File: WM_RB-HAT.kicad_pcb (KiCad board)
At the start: 4 copper layers, 65 x 40.5 mm, 61 parts, among them J1 AudioJack3, J2 AudioJack3, J3 2x20 Pins, J4 AudioJack3, J5 AudioJack3, J6 Audio In, J7 Audio Out, Q1 BC817, U1 WM8960, U4 MCP1711T-33 /OT

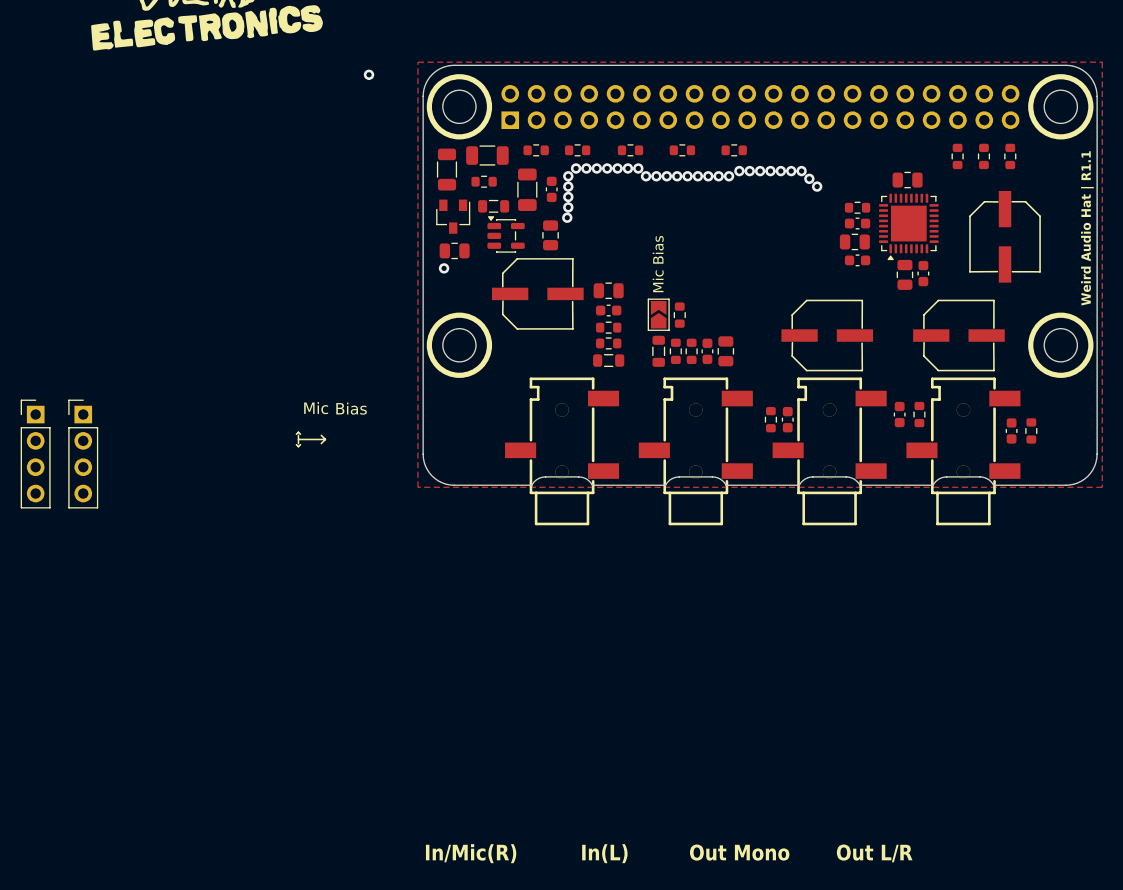
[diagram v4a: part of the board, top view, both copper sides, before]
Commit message: Resize PCB to Raspberry Pi Zero footprint
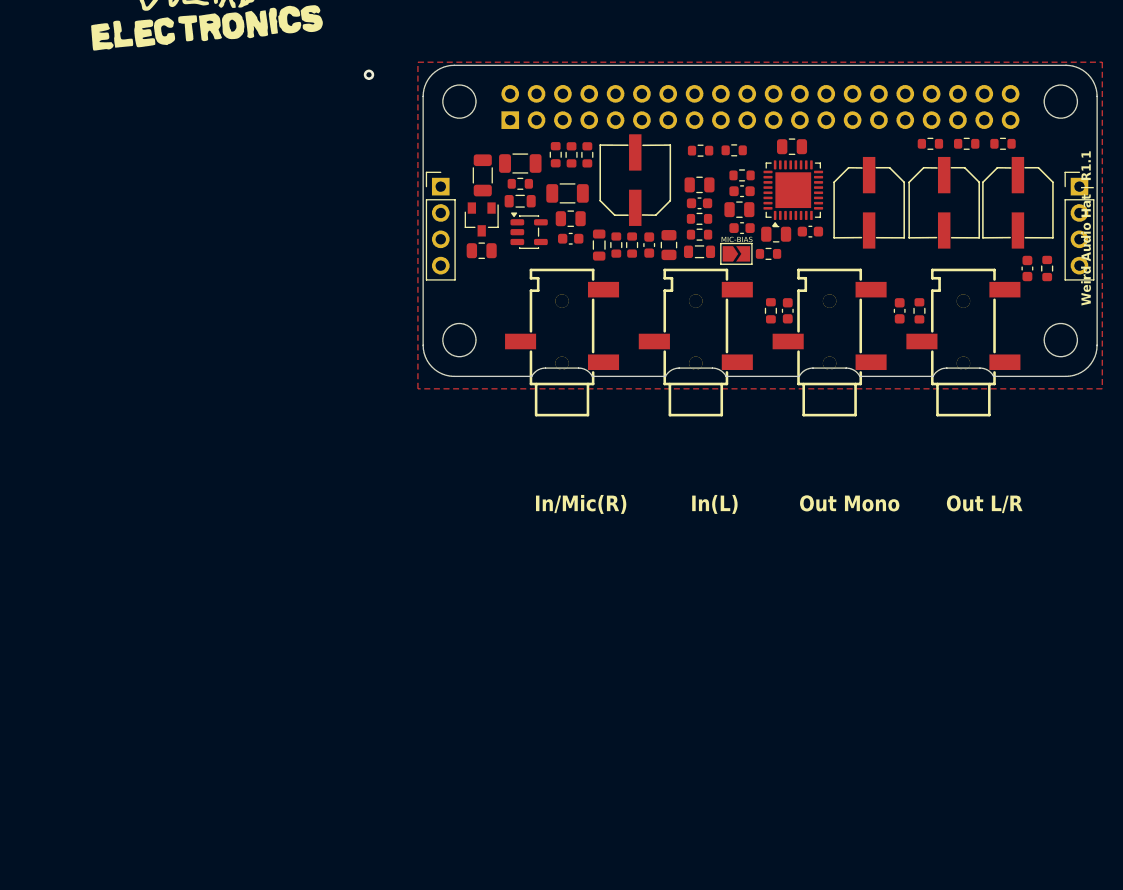
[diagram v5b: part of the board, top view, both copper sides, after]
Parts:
- JP1: value Mic Bias -> MIC-BIAS
- moved J7 98.6 mm to (141.8, 72.0)
- moved J6 44.8 mm to (80.2, 72.0)
- moved C18 16.3 mm to (105.2, 71.8), turned to 180 degrees
- moved C29 15.7 mm to (136.8, 79.9)
- moved R22 15.7 mm to (138.7, 79.9)
- moved CP3 14.4 mm to (99.0, 71.4), turned to 90 degrees
- moved C21 14.3 mm to (105.2, 73.6), turned to 0 degrees
- moved CP2 14.0 mm to (135.9, 73.6), turned to -90 degrees
- moved CP4 13.4 mm to (121.5, 73.6), turned to -90 degrees
- moved C2 13.0 mm to (112.5, 76.6), turned to 0 degrees
- moved R8 12.8 mm to (105.2, 75.1), turned to 0 degrees
- moved C3 11.6 mm to (115.8, 76.3), turned to 180 degrees
- moved C8 11.6 mm to (114.1, 68.1)
- moved U1 11.6 mm to (114.2, 72.3)
- moved C5 11.6 mm to (109.3, 76.0)
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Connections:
- J6 pad 2: /INPUT_R -> /LINE_INPUT_R
- J6 pad 4: /INPUT_L -> /LINE_INPUT_L
- J7 pad 2: /OUTPUT_R -> /HP_R_AC
- J7 pad 4: /OUTPUT_L -> /HP_L_AC
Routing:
- net GND: vias 32 -> 1
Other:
- board size 65 x 40.5 mm -> 65 x 30 mm
- board text removed: "Bias"
- board text removed: "Mic"

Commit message: PCB layout adjustments
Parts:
- G*** (x2): moved to B.Cu
- moved G*** 61.2 mm to (112.1, 81.0), turned to 172 degrees
- moved G*** 52.8 mm to (109.9, 73.6), turned to 180 degrees

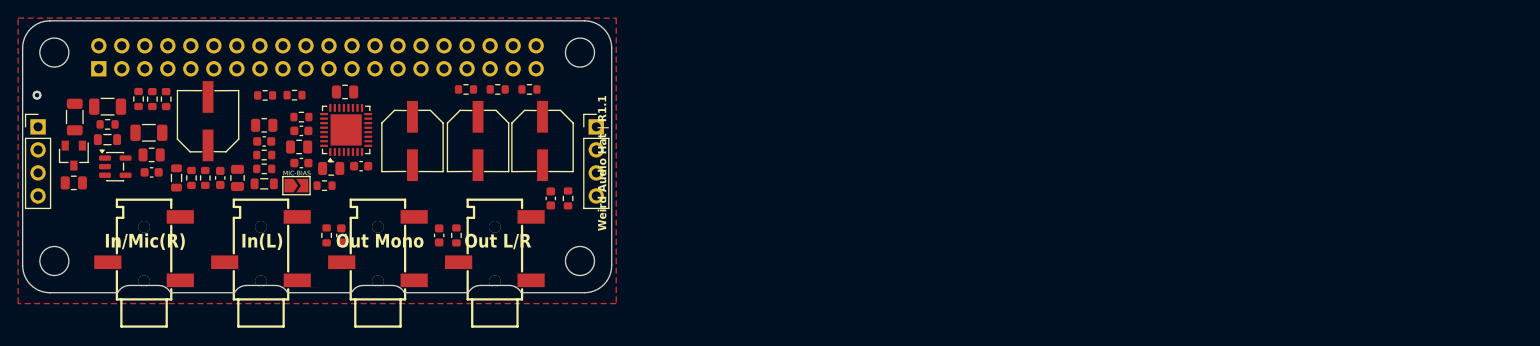
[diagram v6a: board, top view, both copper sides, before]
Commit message: Add SSSS213202 slide switch library, PCB and schematic updates
- Add Alps SSSS213202 SPDT switch: symbol, footprint, 3D model (LCSC C115375)
- Register switch libraries in sym-lib-table and fp-lib-table
- Schematic and PCB layout updates
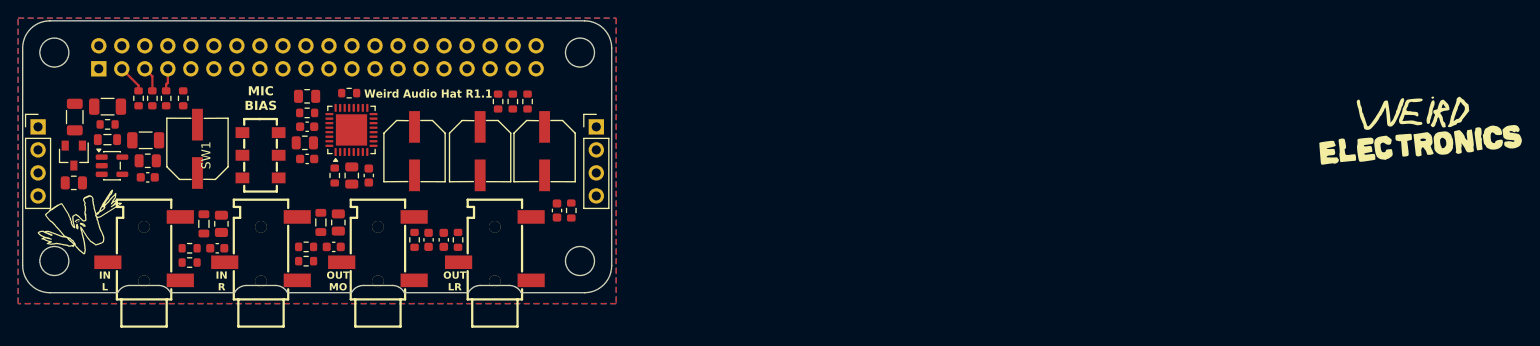
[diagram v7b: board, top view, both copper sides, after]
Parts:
- removed JP1: MIC-BIAS, ArduinoModules:SolderJumper-2_P1.3mm_Open_TrianglePad1.0x1.5mm
- added SW1: SSSS213202, SSSS213202:SW-TH_SSSS213202, F.Cu at (104.7, 75.1)
- G*** (x2): moved to F.Cu
- moved G*** 120.3 mm to (232.1, 71.7), turned to 8 degrees
- moved G*** 26.2 mm to (85.2, 82.4), turned to 39 degrees
- moved C21 13.9 mm to (112.8, 85.2), turned to 180 degrees
- moved C18 13.5 mm to (113.3, 82.5), turned to 90 degrees
- moved R8 12.6 mm to (109.8, 86.8)
- moved R9 9.77 mm to (109.8, 85.2)
- moved R6 9.72 mm to (121.7, 84.5)
- moved C9 9.64 mm to (123.3, 84.5)
- moved R7 9.49 mm to (96.9, 87.0), turned to 0 degrees
- moved R2 9.05 mm to (96.2, 68.8), turned to 90 degrees
- moved C20 7.77 mm to (100.0, 85.4), turned to 180 degrees
- moved R10 7.76 mm to (96.9, 85.4), turned to 180 degrees
- moved FB1 7.56 mm to (111.4, 82.5), turned to -90 degrees
- moved R27 6.03 mm to (114.5, 68.3)
- moved FB2 5.90 mm to (98.5, 82.7), turned to -90 degrees
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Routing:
- net /I2C_SDA: track 0.00 -> 3.29 mm
- net /I2C_SCL: track 0.00 -> 2.87 mm
- net Net-(J3-BCM4/GPCLK0): track 0.00 -> 2.60 mm
- net GND: vias 1 -> 0
- added copper zone on B.Cu, net GND
- added copper zone on In2.Cu, net GND
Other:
- board text added: "IN L"
- board text added: "IN R"
- board text added: "MIC BIAS"
- board text added: "OUT LR"
- board text added: "OUT MO"
- board text added: "Weird Audio Hat R1.1"
- board text removed: "In(L)"
- board text removed: "In/Mic(R)"
- board text removed: "Out L/R"
- board text removed: "Out Mono"
- board text removed: "Weird Audio Hat | R1.1"

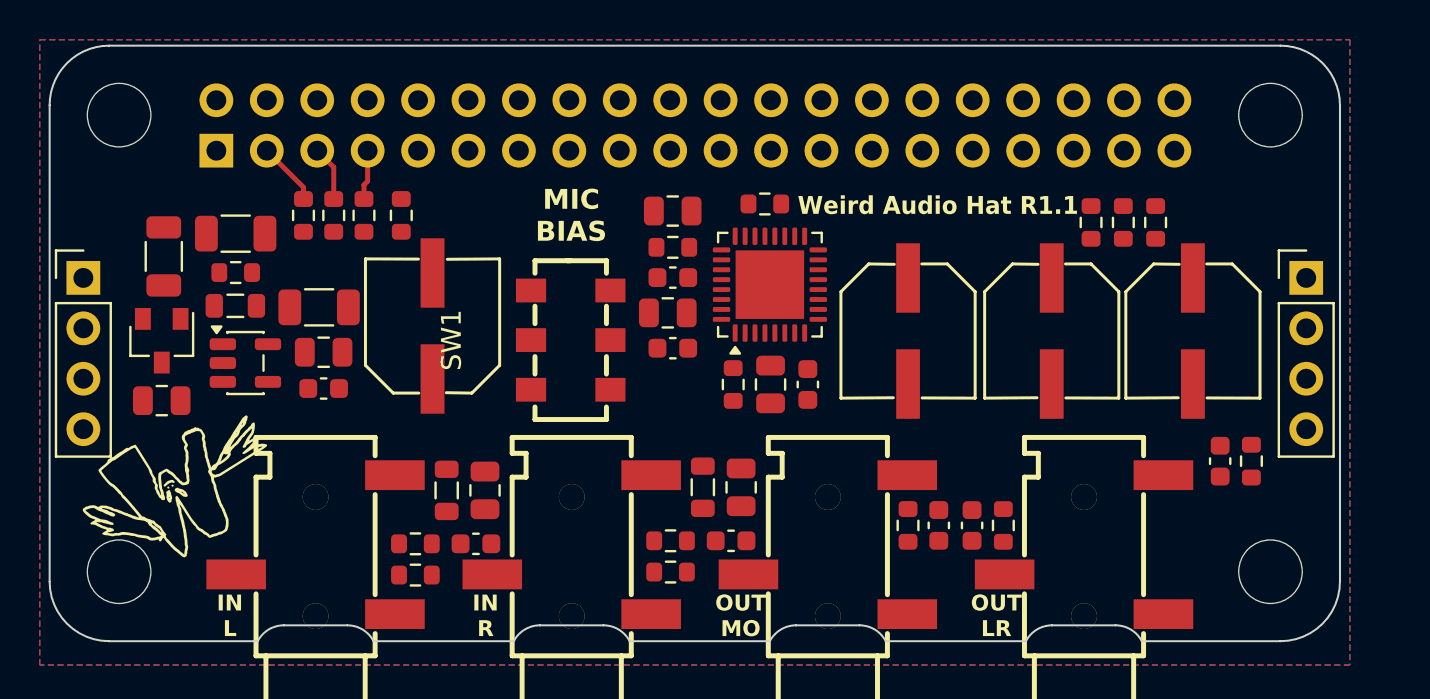
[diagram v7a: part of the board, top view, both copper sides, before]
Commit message: PCB routing progress, fix C36 VMID cap to 4.7uF X7R
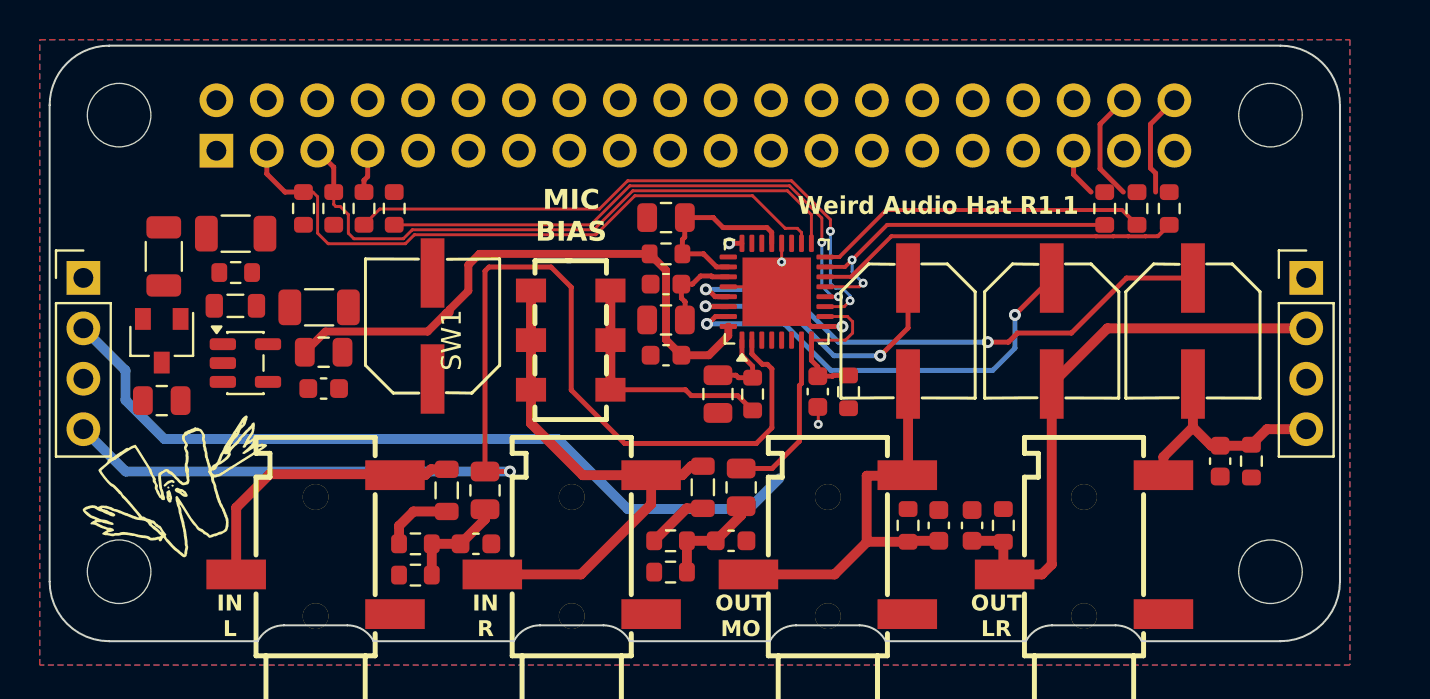
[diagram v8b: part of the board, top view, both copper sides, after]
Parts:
- moved R27 10.4 mm to (118.7, 77.7), turned to -90 degrees
- moved C2 2.69 mm to (112.2, 77.9)
- moved R15 1.09 mm to (113.9, 77.9)
- moved R3 0.98 mm to (134.9, 68.5)
- moved R4 0.98 mm to (131.6, 68.5)
- moved R5 0.98 mm to (133.3, 68.5)
- moved C3 0.61 mm to (117.2, 77.7)
- moved R2 0.50 mm to (95.9, 68.5)
- moved C5 0.49 mm to (109.5, 75.9)
- moved U1 0.49 mm to (115.1, 72.7)
- moved C7 0.48 mm to (109.5, 72.3)
- moved R24 0.48 mm to (109.5, 70.8)
- moved C8 0.47 mm to (109.5, 69.0)
- moved C36 0.37 mm to (109.5, 74.1)
- moved R13 0.35 mm to (92.8, 68.5)
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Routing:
- net /LINE_INPUT_L: track 0.00 -> 60.3 mm, vias 0 -> 1
- net /LINE_INPUT_R: track 0.00 -> 49.0 mm
- net /CLK: track 0.00 -> 31.3 mm, vias 0 -> 2
- net /I2C_SDA: track 3.29 -> 32.9 mm
- net +3.3VA: track 0.00 -> 29.3 mm
- net /HP_R_AC: track 0.00 -> 28.9 mm
- net /HP_L: track 0.00 -> 28.8 mm, vias 0 -> 2
- net /I2C_SCL: track 2.87 -> 31.3 mm
- net Net-(U1-BCLK): track 0.00 -> 28.2 mm, vias 0 -> 2
- net /INPUT_R: track 0.00 -> 27.5 mm
- net /HP_R: track 0.00 -> 22.5 mm, vias 0 -> 2
- net /OUT_MONO_AC: track 0.00 -> 20.3 mm
- net Net-(U1-DACAT): track 0.00 -> 18.4 mm
- net Net-(U1-ADCLRC/GPIO1): track 0.00 -> 18.4 mm, vias 0 -> 2
- net Net-(U1-ADCDAT): track 0.00 -> 17.0 mm
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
